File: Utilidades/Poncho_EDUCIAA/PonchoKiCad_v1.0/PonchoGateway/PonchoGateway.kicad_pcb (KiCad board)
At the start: 2 copper layers, 1 part, among them SW1 SW_Push

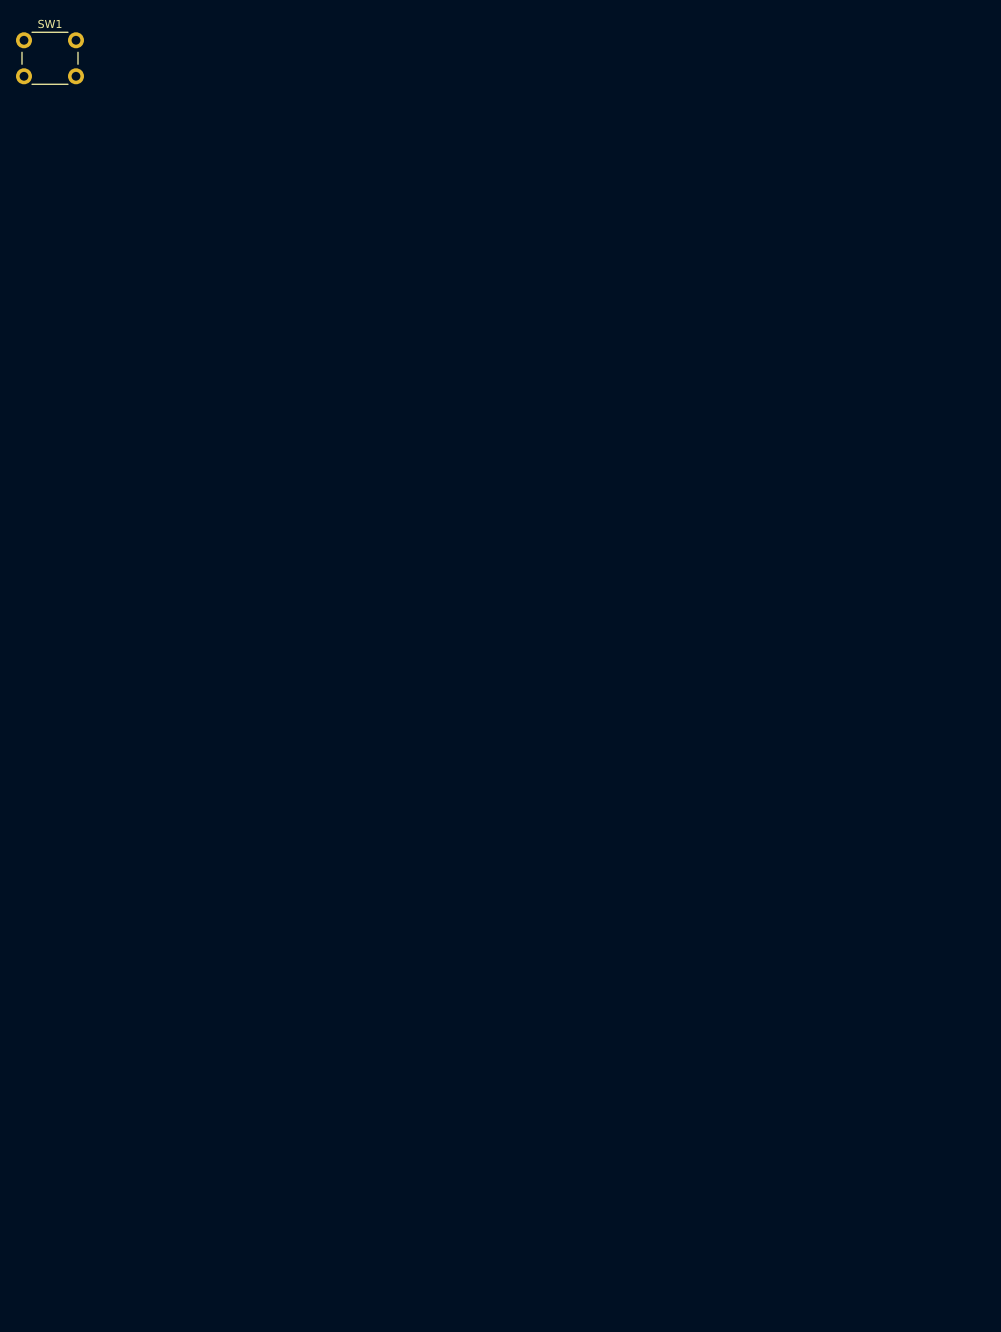
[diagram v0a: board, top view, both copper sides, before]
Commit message: Arreglo PonchoGateway, corrijo huellas y ubico componentes en la placa final.
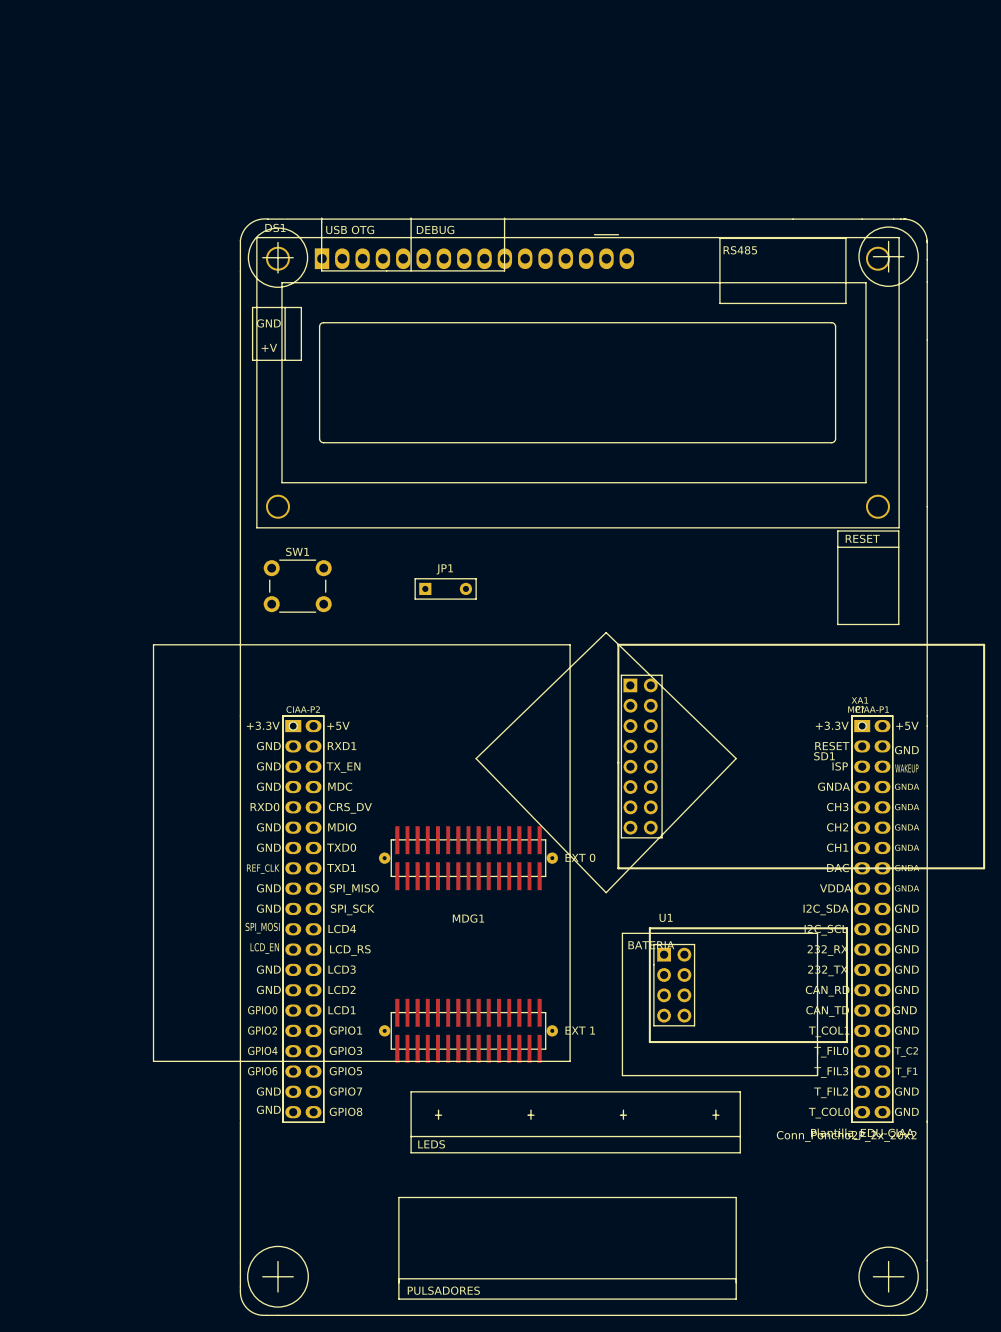
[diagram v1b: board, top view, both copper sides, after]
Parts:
- added DS1: HY1602E, Display:Display_Propio, F.Cu at (75.3, 56.5)
- added JP1: Jumper, lib-ESP8266:JUMPER-PONCHO-EDU-CIAA, F.Cu at (90.8, 95.2)
- added MDG1: MOTEDRESDENGAT_v1, Connector_Samtec_HLE_SMD:SAMTEC-EDU-CIAA, F.Cu at (93.7, 153.0)
- added MP?: Plantilla_EDU-CIAA, Poncho_Esqueleto:Plantilla_EDU-CIAA, F.Cu at (142.9, 114.9)
- added SD1: SD_Arduino, lib-ESP8266:SD-SHIELD-ARD, F.Cu at (112.4, 104.8)
- added U1: ESP-01v090, lib-ESP8266:ESP-01, F.Cu at (118.1, 143.5)
- added XA1: Conn_Poncho2P_2x_20x2, Poncho_Esqueleto:Conn_Poncho_SinBorde, F.Cu at (142.9, 114.9)
- moved SW1 72.9 mm to (69.1, 95.2)
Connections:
- SW1 pad 1: Net-(SW1-Pad1) -> RESET-MOTE
- SW1 pad 2: Net-(SW1-Pad2) -> GND

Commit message: Subo esquemático del ESP8266, y se modifica el PCB de poncho EDU-CIAA-Gateway.
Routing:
- net GND: track 0.00 -> 5.03 mm

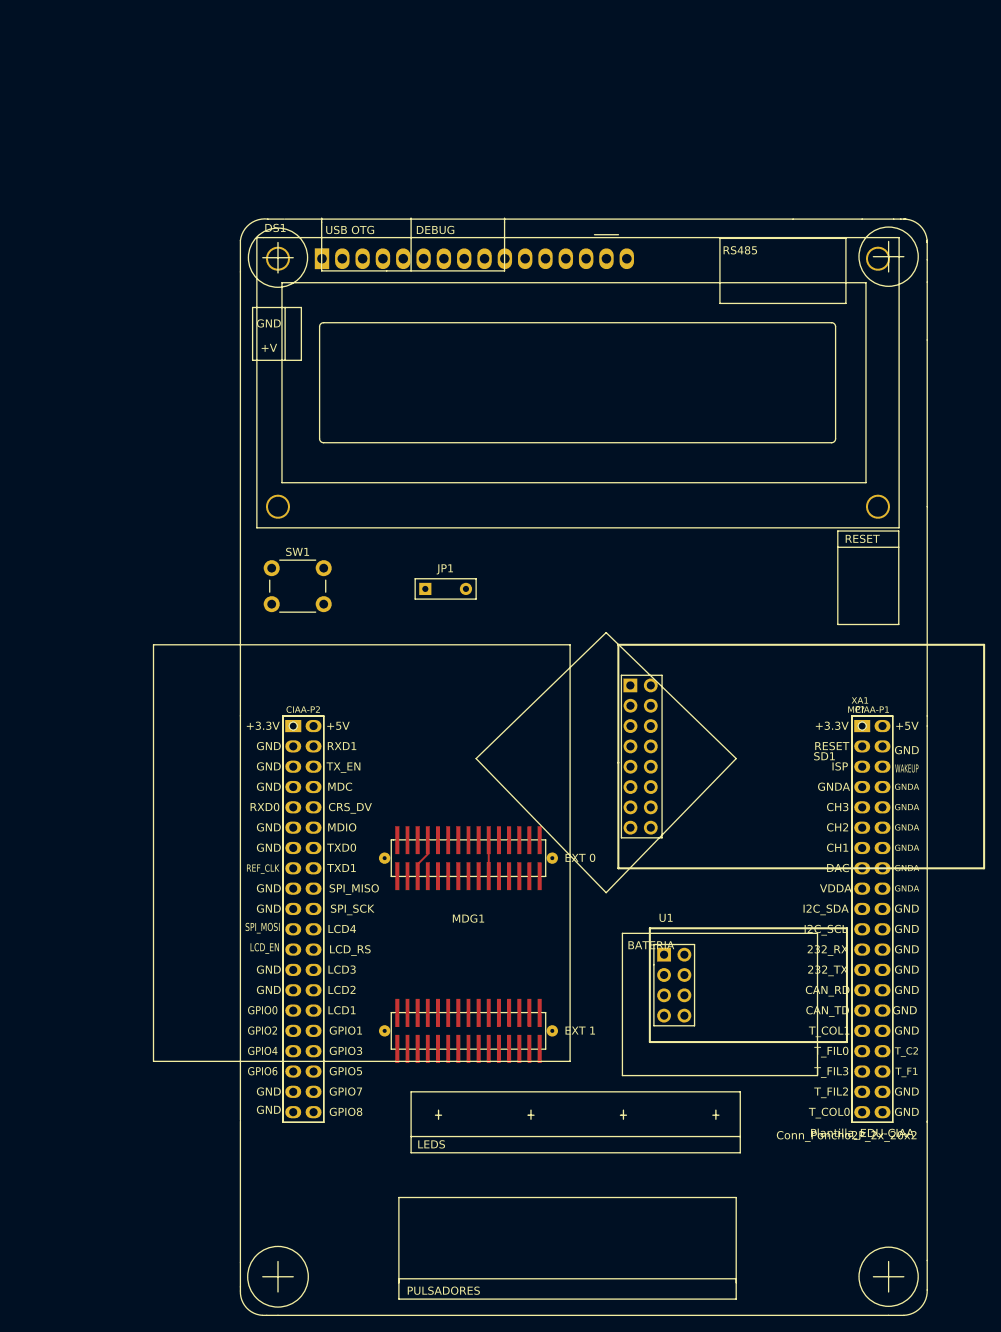
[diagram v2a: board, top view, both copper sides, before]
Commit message: Se corrige error en esquemático, y se termina el pcb.
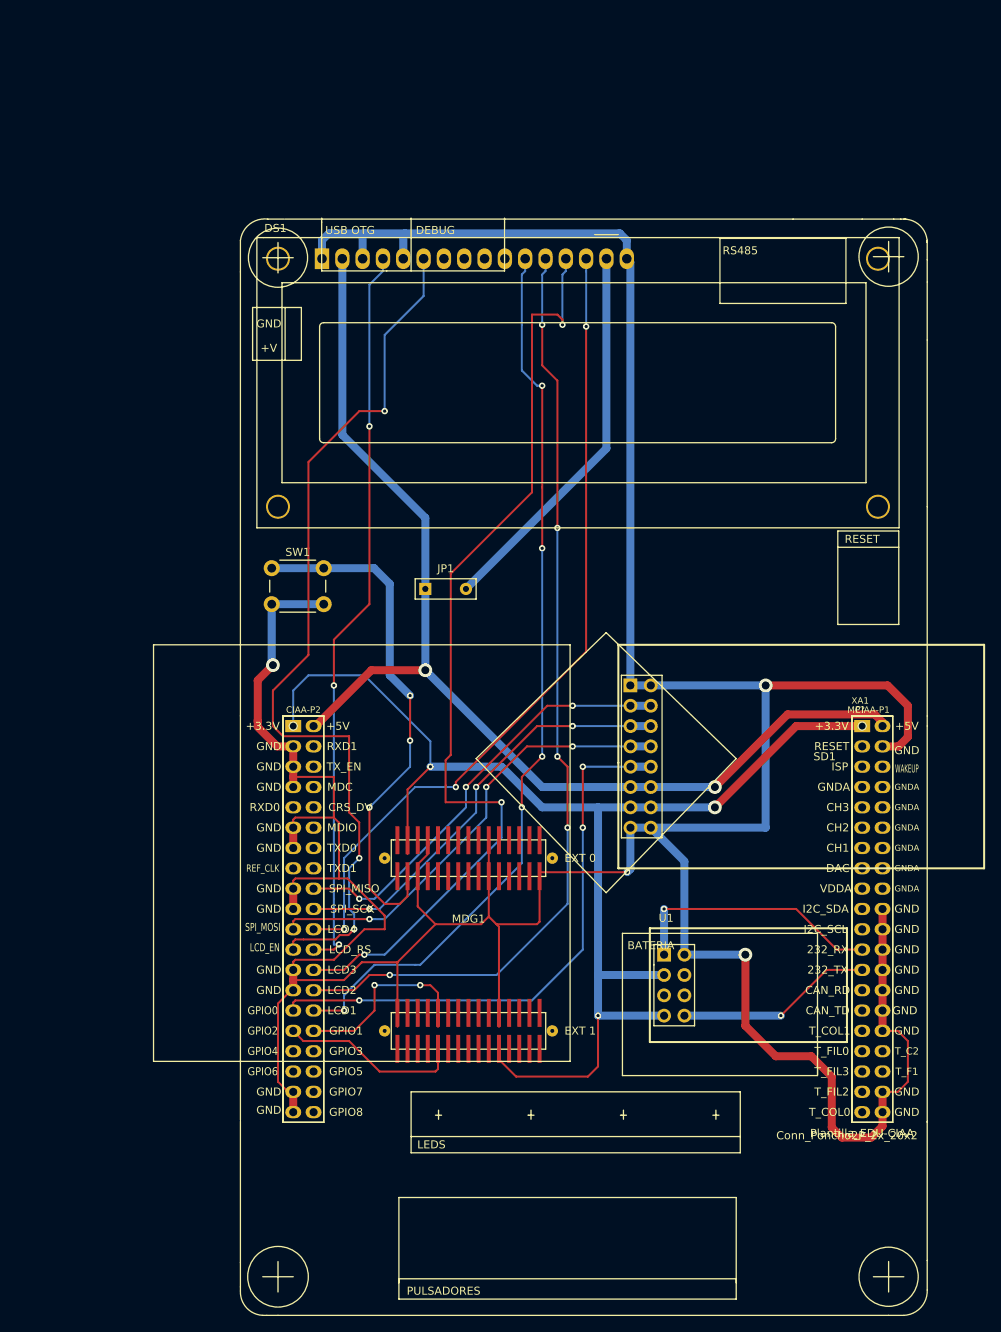
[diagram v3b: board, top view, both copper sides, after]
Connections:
- U1 pad 1: UART-MOTE-TX -> CIAA-UART1-RX
- U1 pad 8: UART-MOTE-RX -> CIAA-UART1-TX
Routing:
- net GND: track 5.03 -> 484.1 mm, vias 0 -> 4
- net +3.3V: track 0.00 -> 165.9 mm, vias 0 -> 3
- net +5V: track 0.00 -> 140.4 mm, vias 0 -> 2
- net LCD3: track 0.00 -> 120.3 mm, vias 0 -> 3
- net LCD2: track 0.00 -> 118.4 mm, vias 0 -> 5
- net LCD1: track 0.00 -> 113.0 mm, vias 0 -> 5
- net LCD-EN: track 0.00 -> 112.8 mm, vias 0 -> 3
- net LCD4: track 0.00 -> 103.1 mm, vias 0 -> 3
- net LCD-RS: track 0.00 -> 92.3 mm, vias 0 -> 3
- net GPIO0-CS: track 0.00 -> 71.3 mm, vias 0 -> 3
- net RESET-MOTE: track 0.00 -> 65.8 mm, vias 0 -> 3
- net CIAA-MOSI: track 0.00 -> 57.0 mm, vias 0 -> 3
- net CIAA-MISO: track 0.00 -> 54.2 mm, vias 0 -> 3
- net CIAA-SCK: track 0.00 -> 53.5 mm, vias 0 -> 3
- net Net-(DS1-Pad2): track 0.00 -> 48.6 mm
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
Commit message: Se agregan Logos en el PonchoGateway, al igual que los power plane referidos a GND en ambas caras.
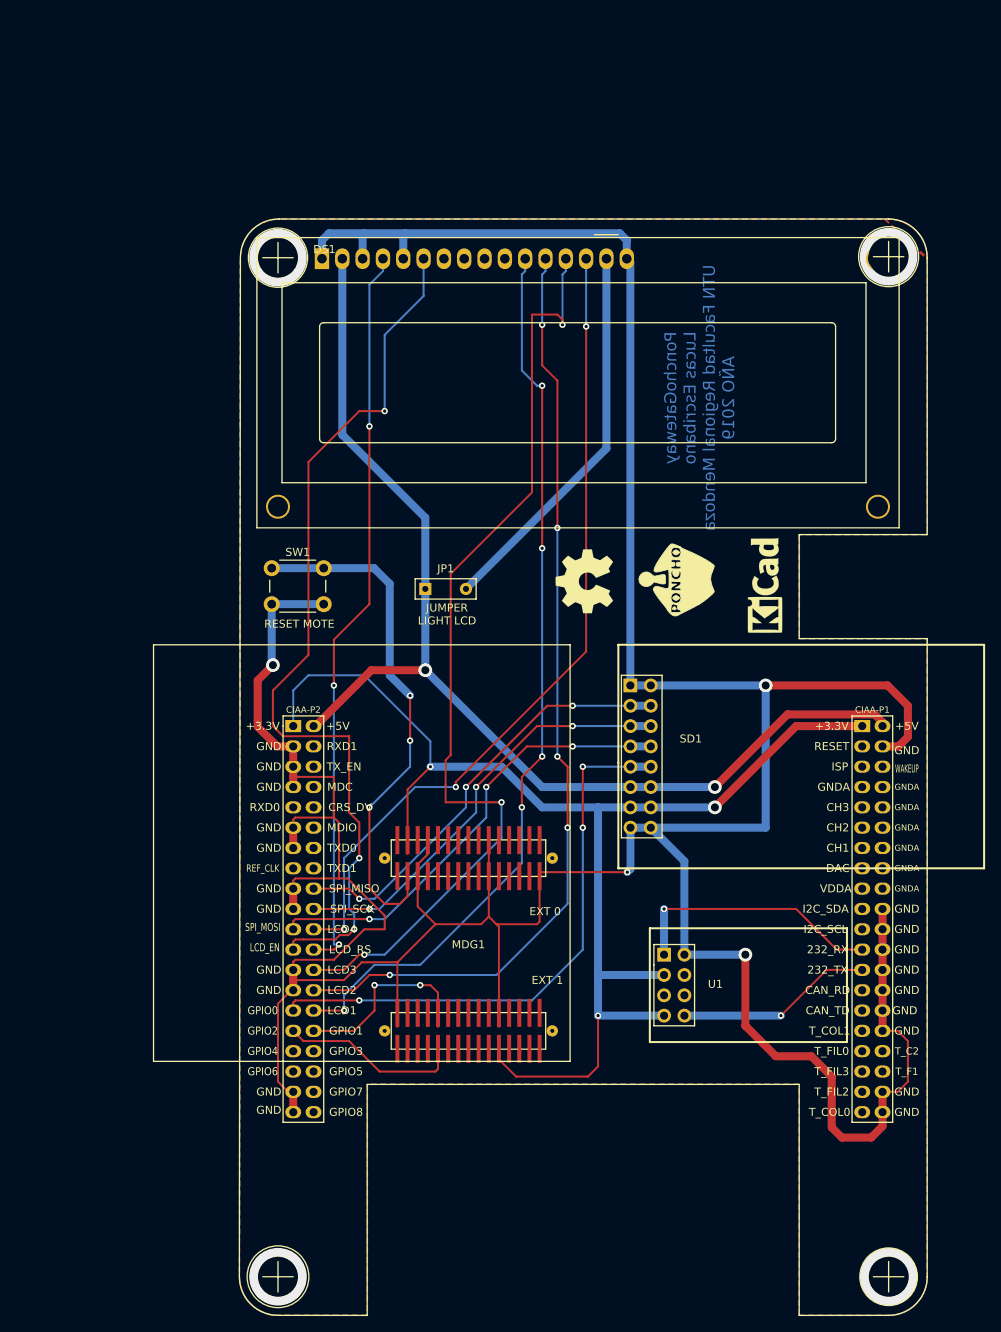
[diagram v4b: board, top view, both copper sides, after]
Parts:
- removed MP?: Plantilla_EDU-CIAA, Poncho_Esqueleto:Plantilla_EDU-CIAA
- added G***: LOGO, Poncho_Esqueleto:gidTICs, B.Cu at (112.2, 74.5)
- added G***: LOGO, Poncho_Esqueleto:logoUTN_chico, B.Cu at (139.0, 79.4)
- added G***: LOGO, Poncho_Esqueleto:Logo_Poncho, F.Cu at (119.7, 96.7)
- added G***: Logo_EDU-CIAA, Poncho_Esqueleto:Logo_EDU-CIAA, B.Cu at (136.4, 65.4)
- added G101: Logo_OSHWA, Poncho_Esqueleto:Logo_OSHWA, F.Cu at (108.1, 96.8)
- added REF**: KiCAD Logo, Poncho_Esqueleto:Symbol_KiCAD-Logo_CopperAndSilkScreenTop, F.Cu at (130.5, 97.3)
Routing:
- net GND: vias 4 -> 7
- net (no net): vias 0 -> 2
- added copper zone on B.Cu, net GND
- added copper zone on F.Cu, net GND
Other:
- board text added: "ESP8266"
- board text added: "JUMPER LIGHT LCD"
- board text added: "PonchoGateway Lucas Escribano UTN Facultad Regional Mendoza AÑO 2019"
- board text added: "RESET MOTE"
- board text added: "SD"

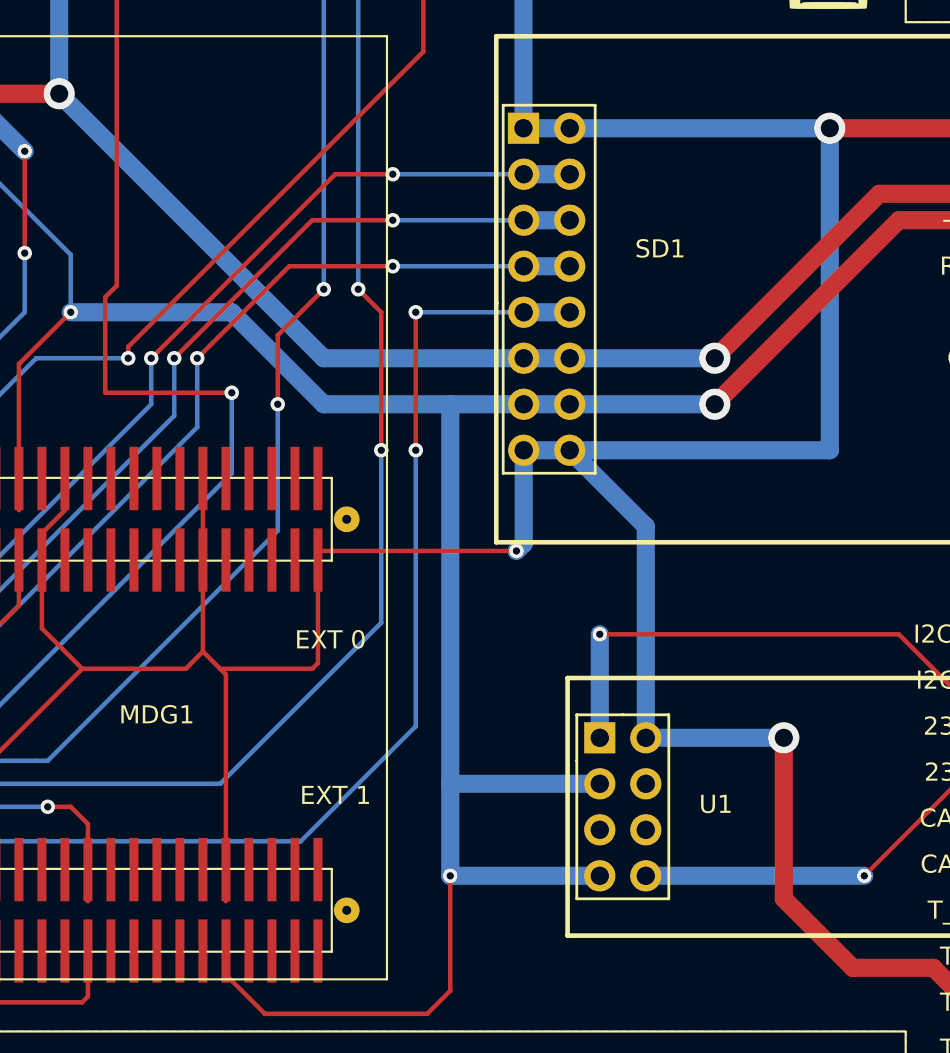
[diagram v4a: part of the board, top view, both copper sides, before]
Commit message: Se corrigen problemas en el SCH y PCB. Se realiza última comprobación antes de hacer la placa.
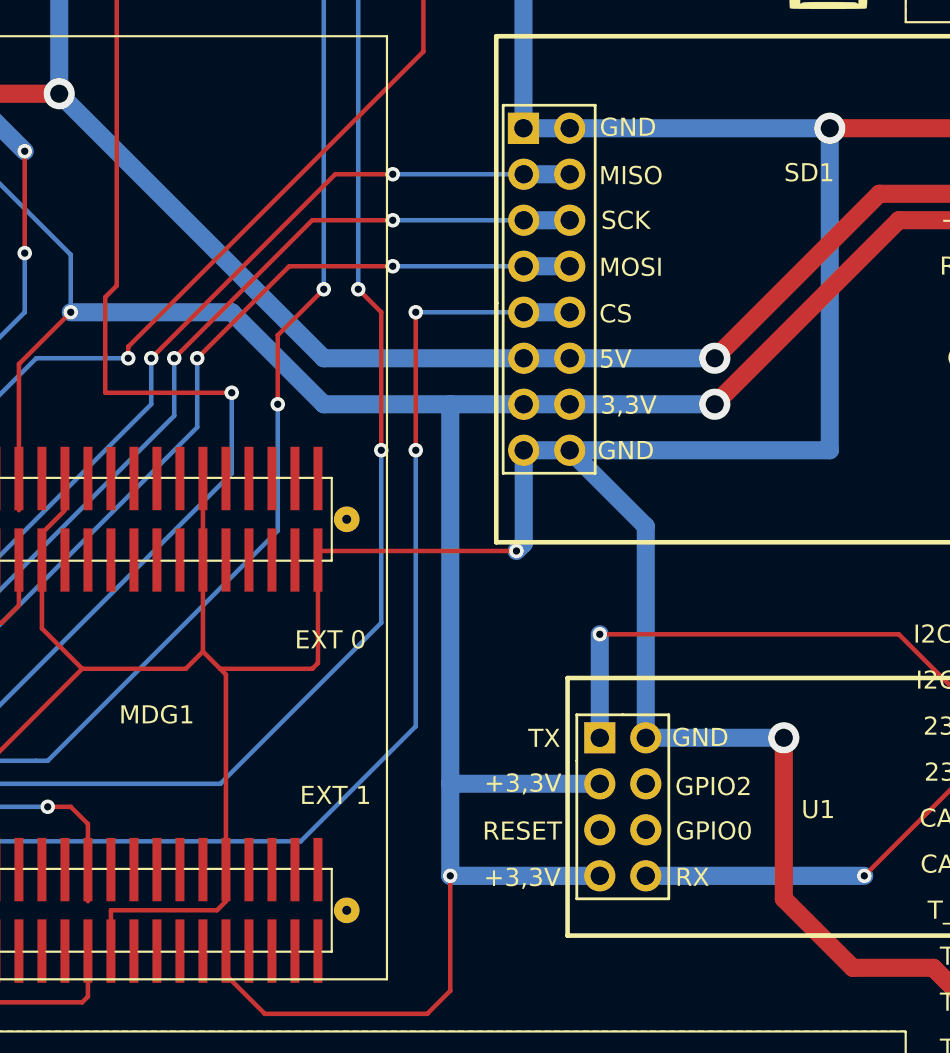
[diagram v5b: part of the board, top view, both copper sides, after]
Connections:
- MDG1 pad 41: Net-(MDG1-Pad41) -> GND
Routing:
- net GND: track 484.1 -> 493.5 mm
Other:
- board text added: "+3,3V"
- board text added: "3,3V"
- board text added: "5V"
- board text added: "CS"
- board text added: "GND"
- board text added: "GPIO0"
- board text added: "GPIO2"
- board text added: "MISO"
- board text added: "MOSI"
- board text added: "RESET"
- board text added: "RX"
- board text added: "SCK"
- board text added: "TX"
